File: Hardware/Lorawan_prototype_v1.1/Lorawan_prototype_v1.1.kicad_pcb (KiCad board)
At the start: 2 copper layers, 100 x 60 mm, 130 parts, among them J1 USB_B_Micro, J2 Barrel_Jack_Switch, J3 Conn_02x05_Odd_Even, J4 USB_B_Micro, J7 THD2528-11SD-GF, Q1 PMOS, Q2 BC846, SW1 SW_SPDT, U1 USBLC6-2SC6, U10 AMS1117-3.3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

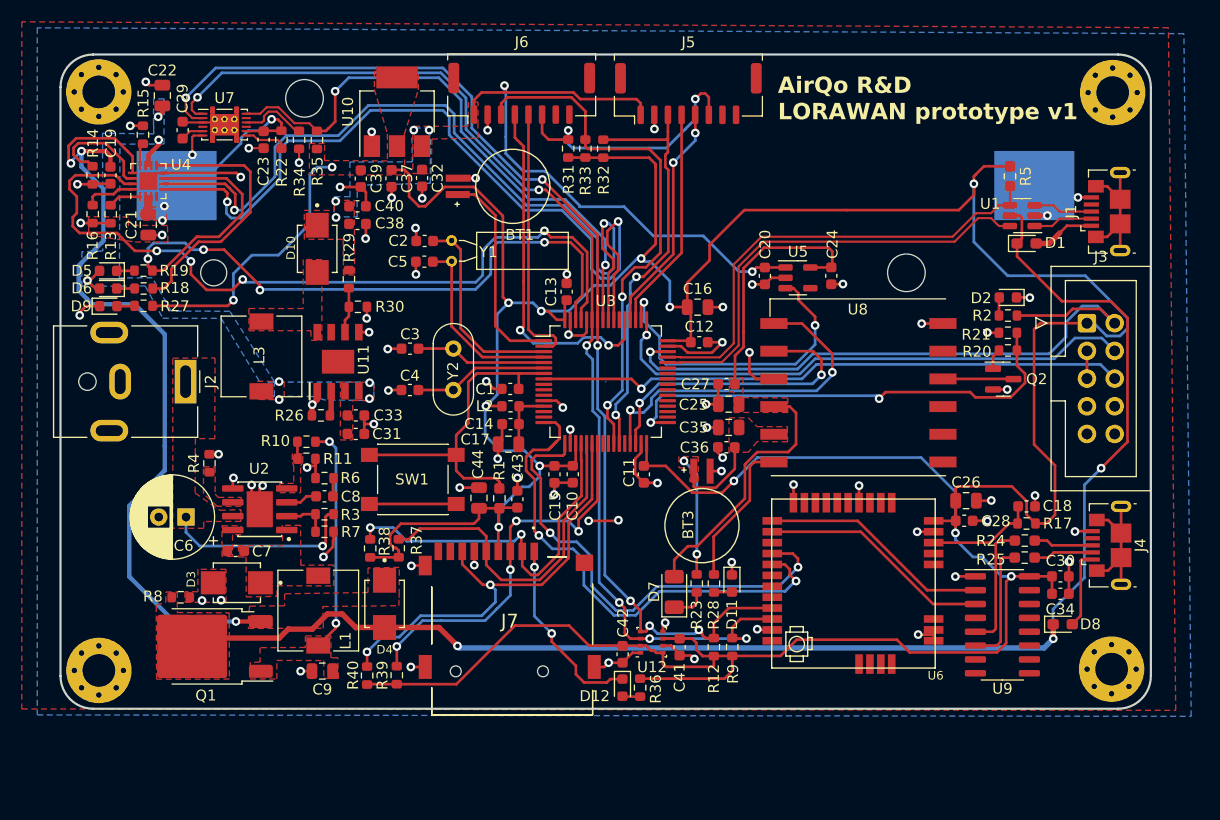
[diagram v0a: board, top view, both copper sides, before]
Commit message: optimized organization of components and routes, and added an i2c expansion pinout
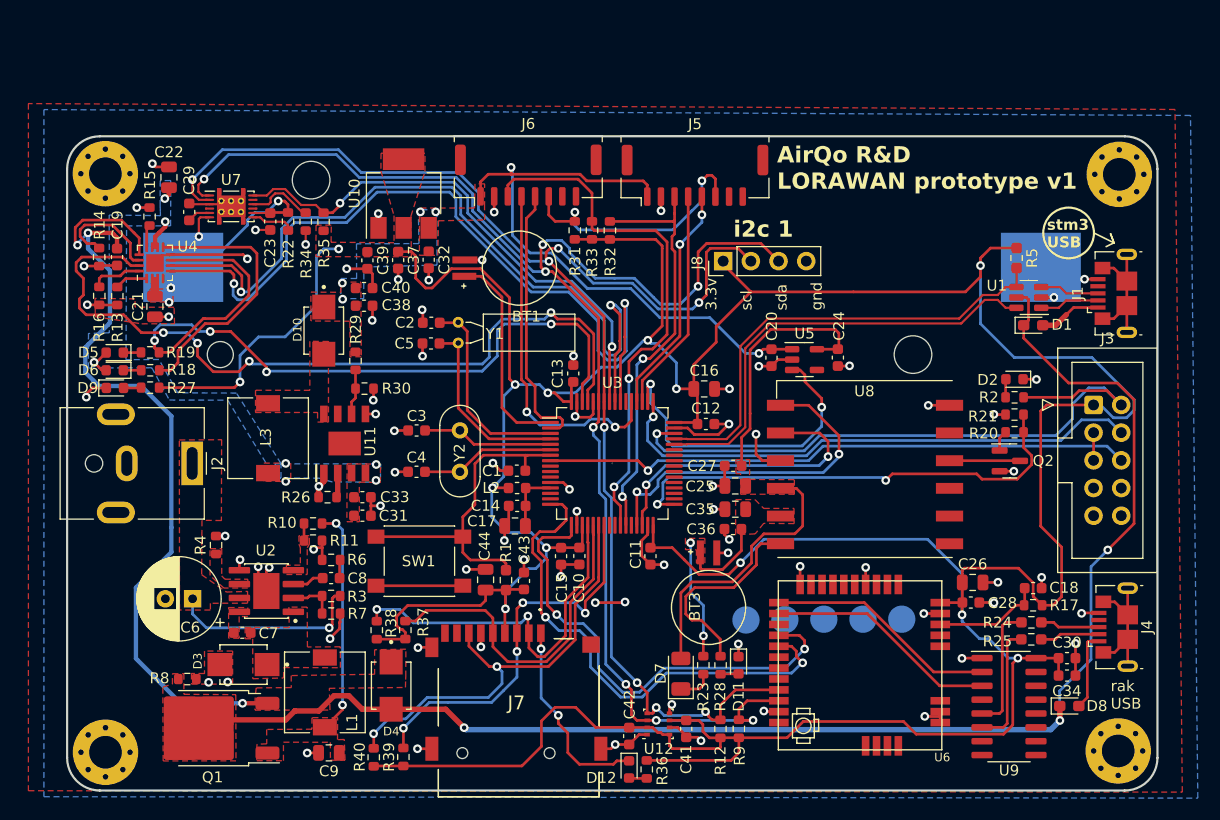
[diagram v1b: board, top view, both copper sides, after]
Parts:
- added J8: Conn_01x04_Pin, Connector_PinHeader_2.54mm:PinHeader_1x04_P2.54mm_Vertical, F.Cu at (159.0, 79.1)
- added REF**: TestPoint_Pad_D2.5mm, TestPoint:TestPoint_Pad_D2.5mm, B.Cu at (168.2, 112.0)
- added REF**: TestPoint_Pad_D2.5mm, TestPoint:TestPoint_Pad_D2.5mm, B.Cu at (171.8, 112.0)
- added REF**: TestPoint_Pad_D2.5mm, TestPoint:TestPoint_Pad_D2.5mm, B.Cu at (164.7, 112.0)
- added REF**: TestPoint_Pad_D2.5mm, TestPoint:TestPoint_Pad_D2.5mm, B.Cu at (175.4, 112.0)
- added REF**: TestPoint_Pad_D2.5mm, TestPoint:TestPoint_Pad_D2.5mm, B.Cu at (161.1, 112.0)
- moved BT3 7.52 mm to (157.7, 110.9)
- moved C11 7.52 mm to (152.3, 106.2)
- moved C12 7.52 mm to (157.4, 94.1)
- moved C14 7.52 mm to (140.1, 101.6)
- moved C15 7.52 mm to (144.1, 106.2)
- moved C17 7.52 mm to (139.9, 103.4)
- moved C25 7.52 mm to (160.1, 99.7)
- moved C27 7.52 mm to (159.9, 97.9)
- moved C30 7.52 mm to (190.5, 115.5)
- moved C34 7.52 mm to (190.5, 117.1)
- moved C36 7.52 mm to (159.9, 103.7)
- moved C41 7.52 mm to (155.6, 122.0)
- moved C42 7.52 mm to (150.4, 122.7)
- moved C43 7.52 mm to (140.7, 108.5)
- moved C8 7.52 mm to (123.1, 108.2)
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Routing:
- net SDA: track 103.3 -> 134.6 mm, vias 6 -> 8
- net SCL: track 103.2 -> 129.7 mm, vias 6 -> 8
- net +3.3V: track 398.5 -> 403.7 mm
- net GPS_IPPS: track 13.7 -> 18.9 mm
- net BAT_STATUS: track 53.0 -> 49.2 mm
- net GPS_3.3V: track 47.9 -> 49.5 mm
- net EN2: track 73.6 -> 72.7 mm
- net UART5_RX: track 24.2 -> 24.9 mm
- net SD_DET: track 17.6 -> 18.2 mm
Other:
- board text added: "3.3v scl sda gnd"
- board text added: "designed at AirQo makerere |okd."
- board text added: "i2c 1"
- board text added: "rak USB"
- board text added: "stm3 USB"

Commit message: optimized placement and routing of componenets
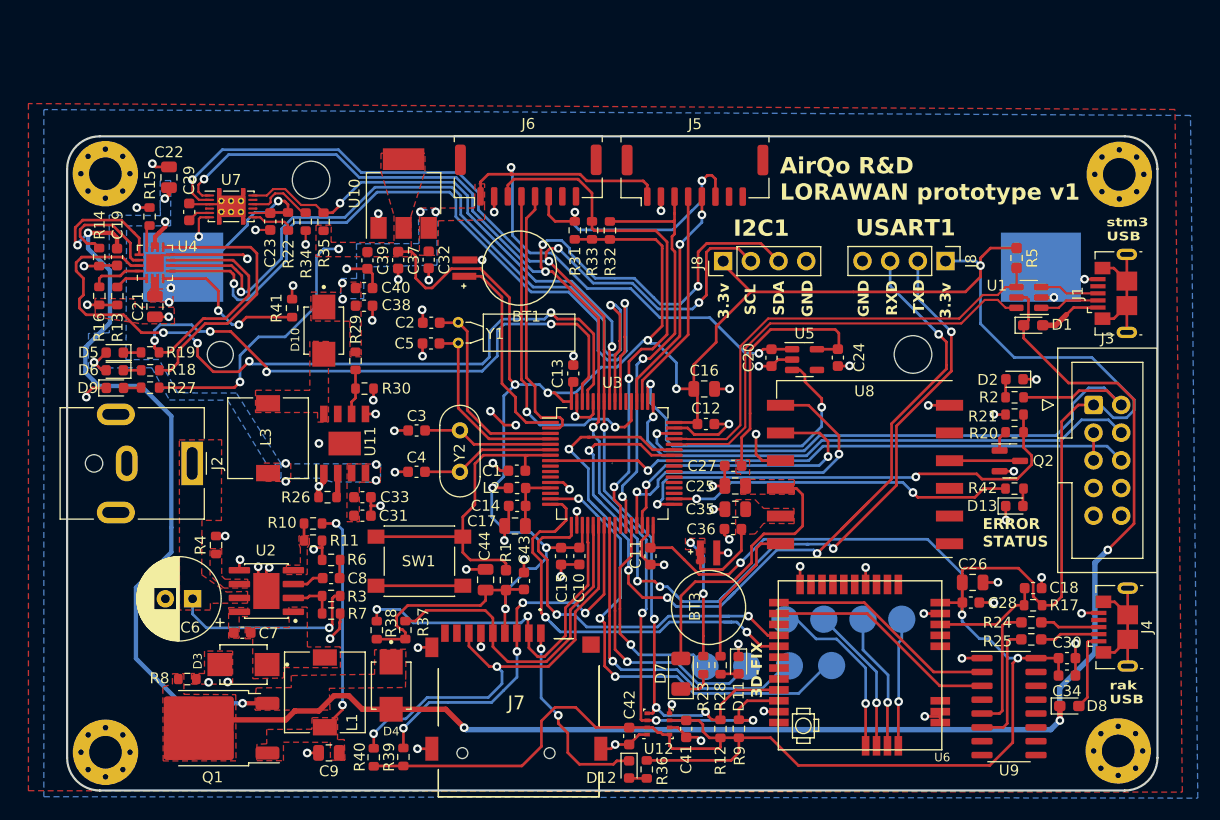
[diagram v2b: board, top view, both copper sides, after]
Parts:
- removed the REF** at (161.1, 112.0)
- added D13: ERROR_STATUS_LED_RED, LED_SMD:LED_0603_1608Metric, F.Cu at (185.7, 101.6)
- added J8: Conn_01x04_Pin, Connector_PinHeader_2.54mm:PinHeader_1x04_P2.54mm_Vertical, F.Cu at (179.4, 79.1)
- added R41: 100k, Resistor_SMD:R_0603_1608Metric, F.Cu at (119.5, 83.4)
- added R42: 1K, Resistor_SMD:R_0603_1608Metric, F.Cu at (185.7, 100.0)
- added REF**: TestPoint_Pad_D2.5mm, TestPoint:TestPoint_Pad_D2.5mm, B.Cu at (157.3, 116.3)
- added REF**: TestPoint_Pad_D2.5mm, TestPoint:TestPoint_Pad_D2.5mm, B.Cu at (165.1, 116.2)
- added REF**: TestPoint_Pad_D2.5mm, TestPoint:TestPoint_Pad_D2.5mm, B.Cu at (161.2, 116.3)
- added REF**: TestPoint_Pad_D2.5mm, TestPoint:TestPoint_Pad_D2.5mm, B.Cu at (168.9, 116.2)
- D6: value LED_RED -> LED_YELLOW
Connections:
- REF** pad 3: (no net) -> MISO_RAK
- REF** pad 4: (no net) -> CLK_RAK
- REF** pad 2: (no net) -> MOSI_RAK
- REF** pad 5: (no net) -> NSS_RAK
- U3 pad 15: unconnected-(U3-PA1-Pad15) -> PA1
- U3 pad 24: unconnected-(U3-PC4-Pad24) -> PC4
- U3 pad 25: unconnected-(U3-PC5-Pad25) -> PC5
- U3 pad 28: unconnected-(U3-PB2-Pad28) -> PB2
- U3 pad 34: unconnected-(U3-PB13-Pad34) -> Net-(U3-PB13)
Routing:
- net USART1_RX: track 0.00 -> 84.4 mm, vias 0 -> 5
- net USART1_TX: track 0.00 -> 77.3 mm, vias 0 -> 5
- net PA1: track 0.00 -> 43.0 mm, vias 0 -> 3
- net Net-(U3-PB13): track 0.00 -> 31.9 mm, vias 0 -> 2
- net PC4: track 0.00 -> 30.2 mm, vias 0 -> 1
- net PC5: track 0.00 -> 25.4 mm, vias 0 -> 1
- net PB2: track 0.00 -> 19.5 mm, vias 0 -> 1
- net MOSI_RAK: track 0.00 -> 16.4 mm, vias 0 -> 1
- net CE: track 0.00 -> 14.9 mm, vias 0 -> 2
- net MISO_RAK: track 0.00 -> 13.6 mm, vias 0 -> 1
- net CLK_RAK: track 0.00 -> 12.6 mm, vias 0 -> 1
- net NSS_RAK: track 0.00 -> 11.7 mm, vias 0 -> 1
- net RAK11720_UART0_TX: track 43.8 -> 34.3 mm
- net RAK11720_UART0_RX: track 47.6 -> 40.2 mm
- net GPS_IPPS: track 18.9 -> 13.7 mm
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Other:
- board text added: "3.3v"
- board text added: "3D-FIX"
- board text added: "ERROR STATUS"
- board text added: "GND"
- board text added: "I2C1"
- board text added: "MISO"
- board text added: "MOSI"
- board text added: "PA1"
- board text added: "PB2"
- board text added: "PC4"
- board text added: "PC5"
- board text added: "RAK11720"
- board text added: "RXD"
- board text added: "SCK"
- board text added: "SCL"
- board text added: "SDA"
- board text added: "SS"
- board text added: "STM32"
- board text added: "TXD"
- board text added: "USART1"
- board text removed: "3.3v scl sda gnd"
- board text removed: "i2c 1"
